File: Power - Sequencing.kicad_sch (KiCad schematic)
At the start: 0 parts

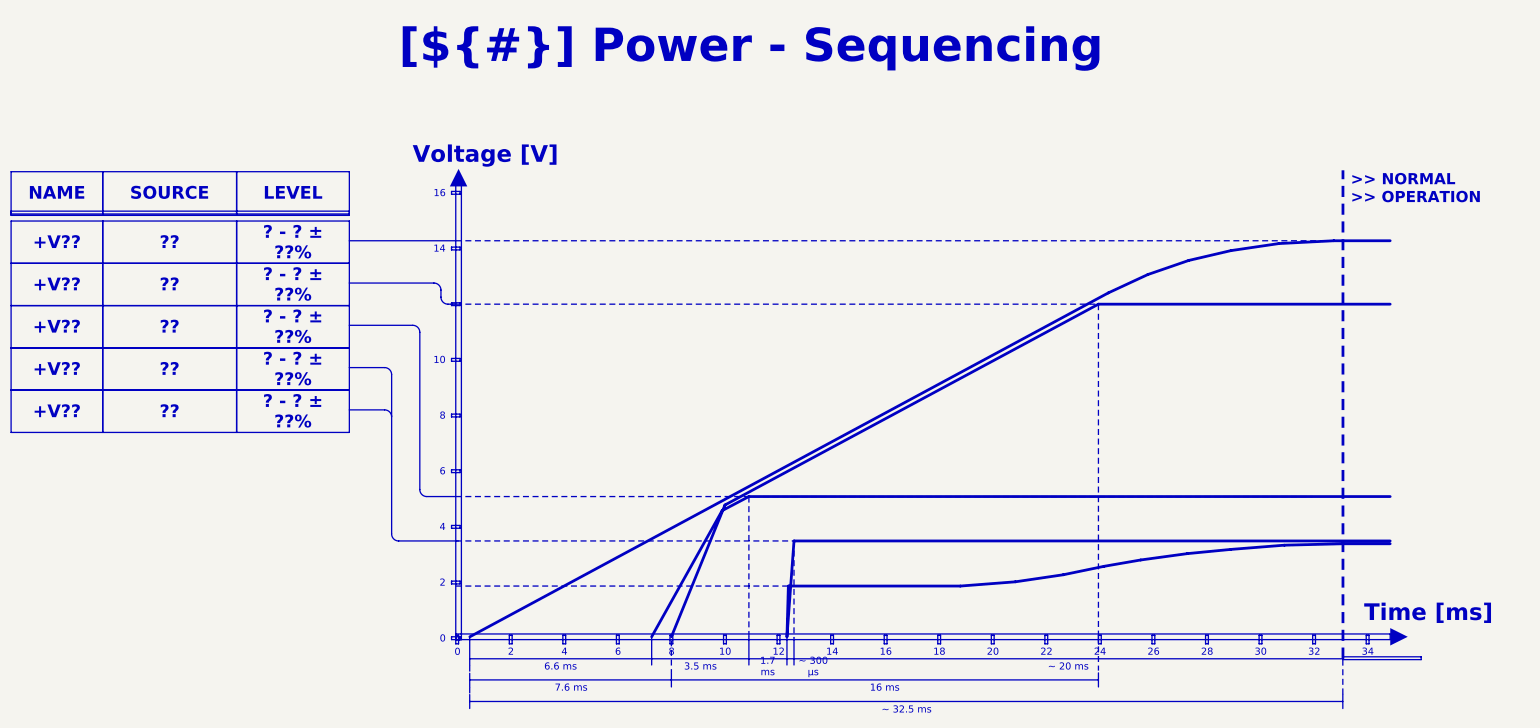
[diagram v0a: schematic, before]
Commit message: [added] completed initial sch design, move from draft to preliminary
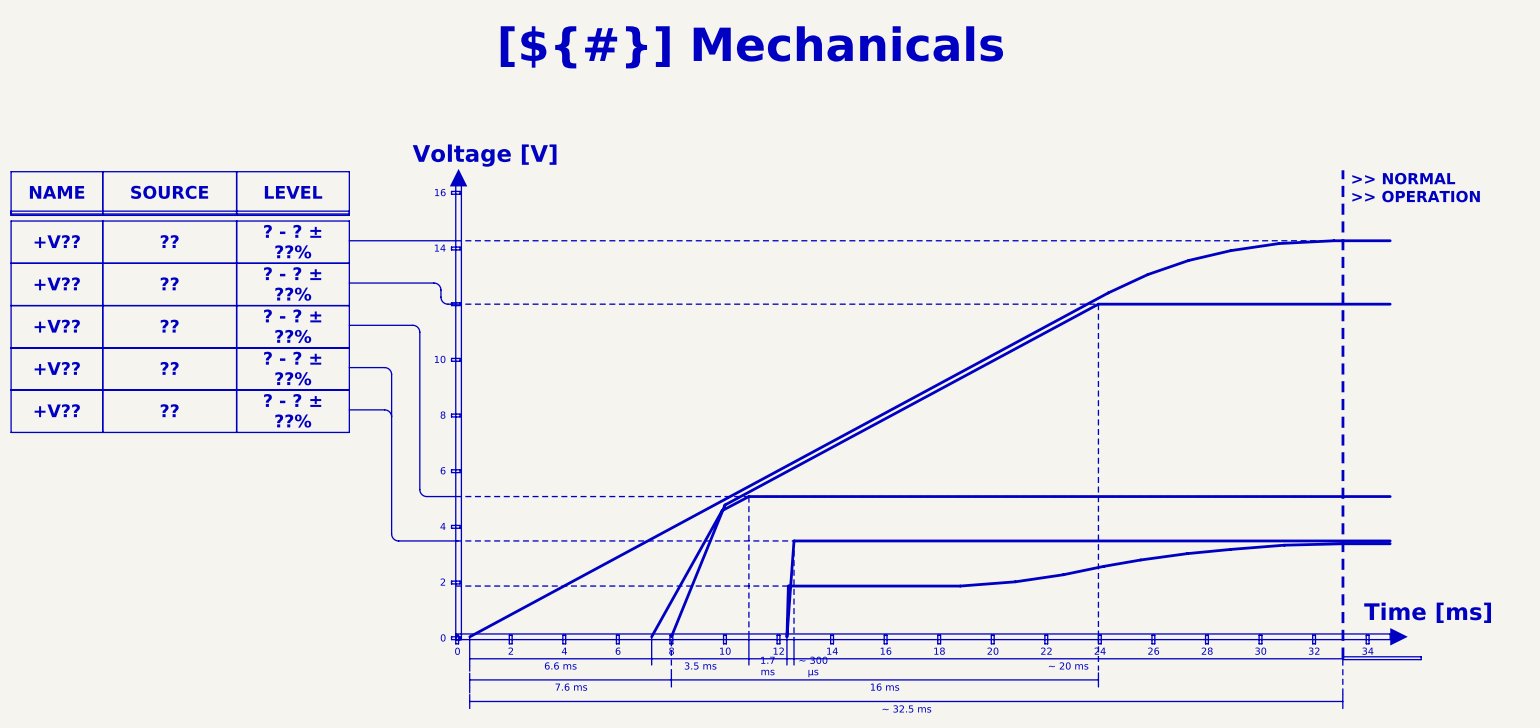
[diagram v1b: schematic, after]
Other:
- title: Power - Sequencing -> Mechanicals
